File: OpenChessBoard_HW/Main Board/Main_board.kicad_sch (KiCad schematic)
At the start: 11 parts, among them U1 74HCT595, U2 74HCT595

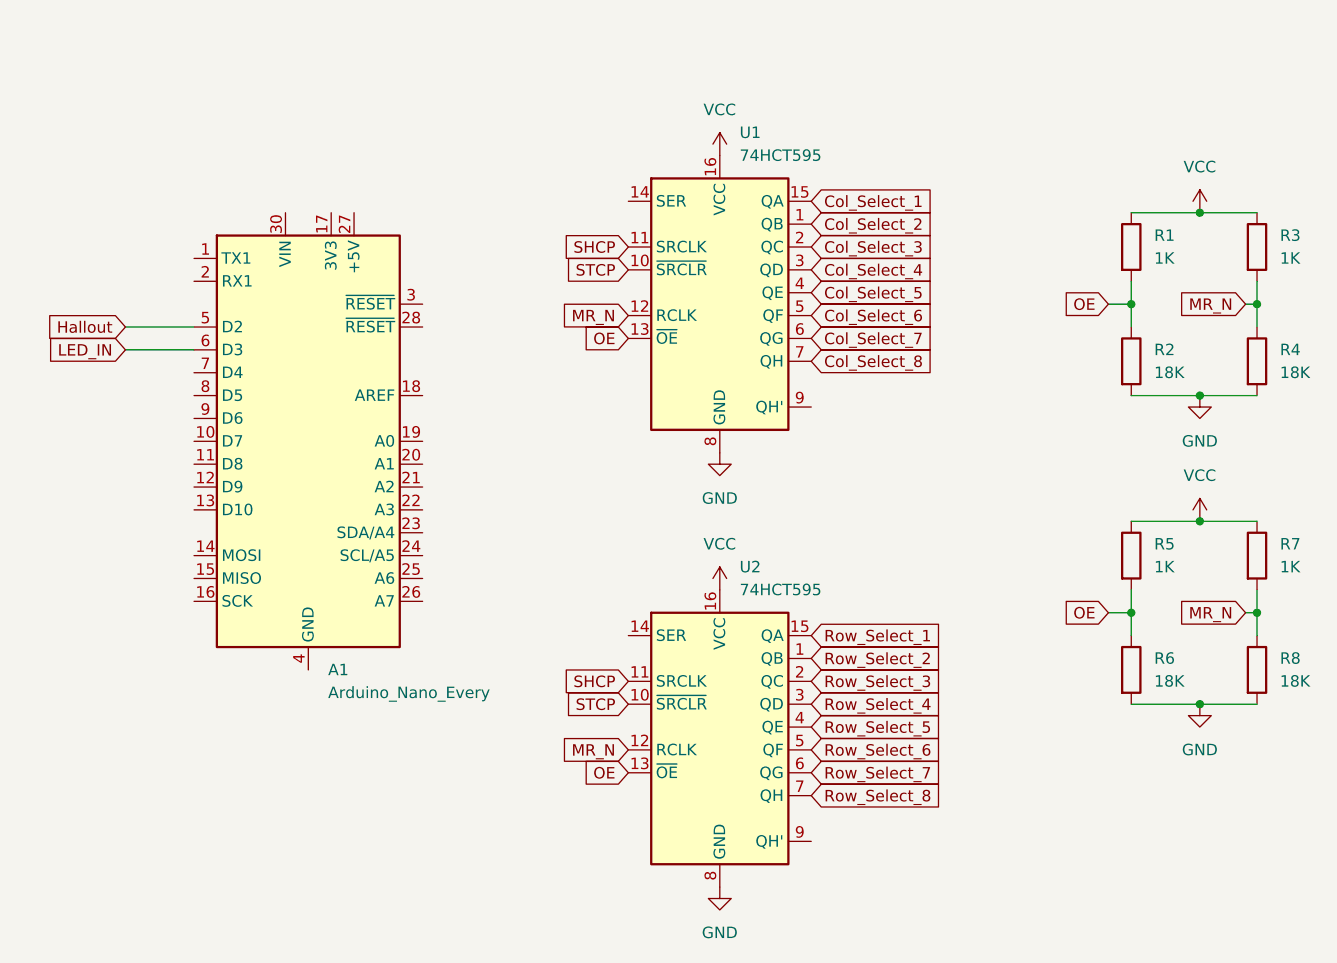
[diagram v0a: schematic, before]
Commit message: Populated Main board Schematic
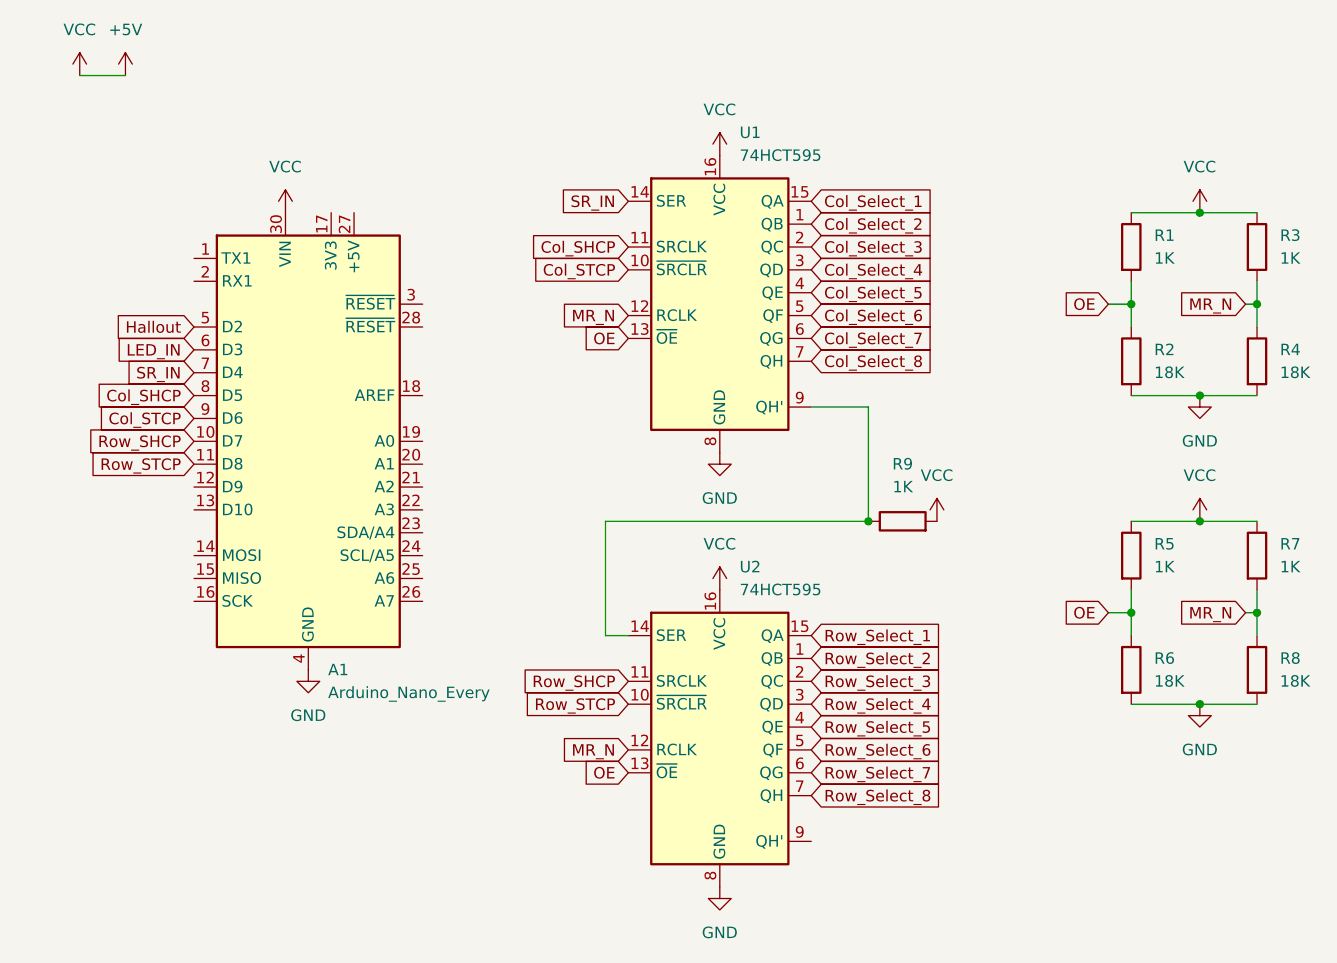
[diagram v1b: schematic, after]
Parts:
- added R9: 1K, Resistor_THT:R_Axial_DIN0204_L3.6mm_D1.6mm_P5.08mm_Horizontal, symbol Device:R
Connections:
- net VCC is gone; now on net +5V: R1.1, R3.1, R5.1, R7.1, U1.16 (VCC), U2.16 (VCC)
- net GND: now also A1.29 (GND), A1.4 (GND)
- net Row_SHCP: now reaches A1.10 (D7)
- net Row_SHCP: now also U2.11 (SRCLK)
- net Row_STCP: now reaches A1.11 (D8)
- net Row_STCP: now also U2.10 (~{SRCLR})
- net +5V: now reaches A1.30 (VIN)
- net +5V: now also R9.2
- net SR_IN: now reaches A1.7 (D4)
- net SR_IN: now also U1.14 (SER)
- net Col_SHCP: now reaches A1.8 (D5)
- net Col_SHCP: now also U1.11 (SRCLK)
- net Col_STCP: now reaches A1.9 (D6)
- net Col_STCP: now also U1.10 (~{SRCLR})
- net at U1.9 (QH'): now also U2.14 (SER), R9.1
- removed net SHCP: U1.11 (SRCLK), U2.11 (SRCLK)
- removed net STCP: U1.10 (~{SRCLR}), U2.10 (~{SRCLR})

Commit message: Update Main board to use 74HCT164 instead of 595
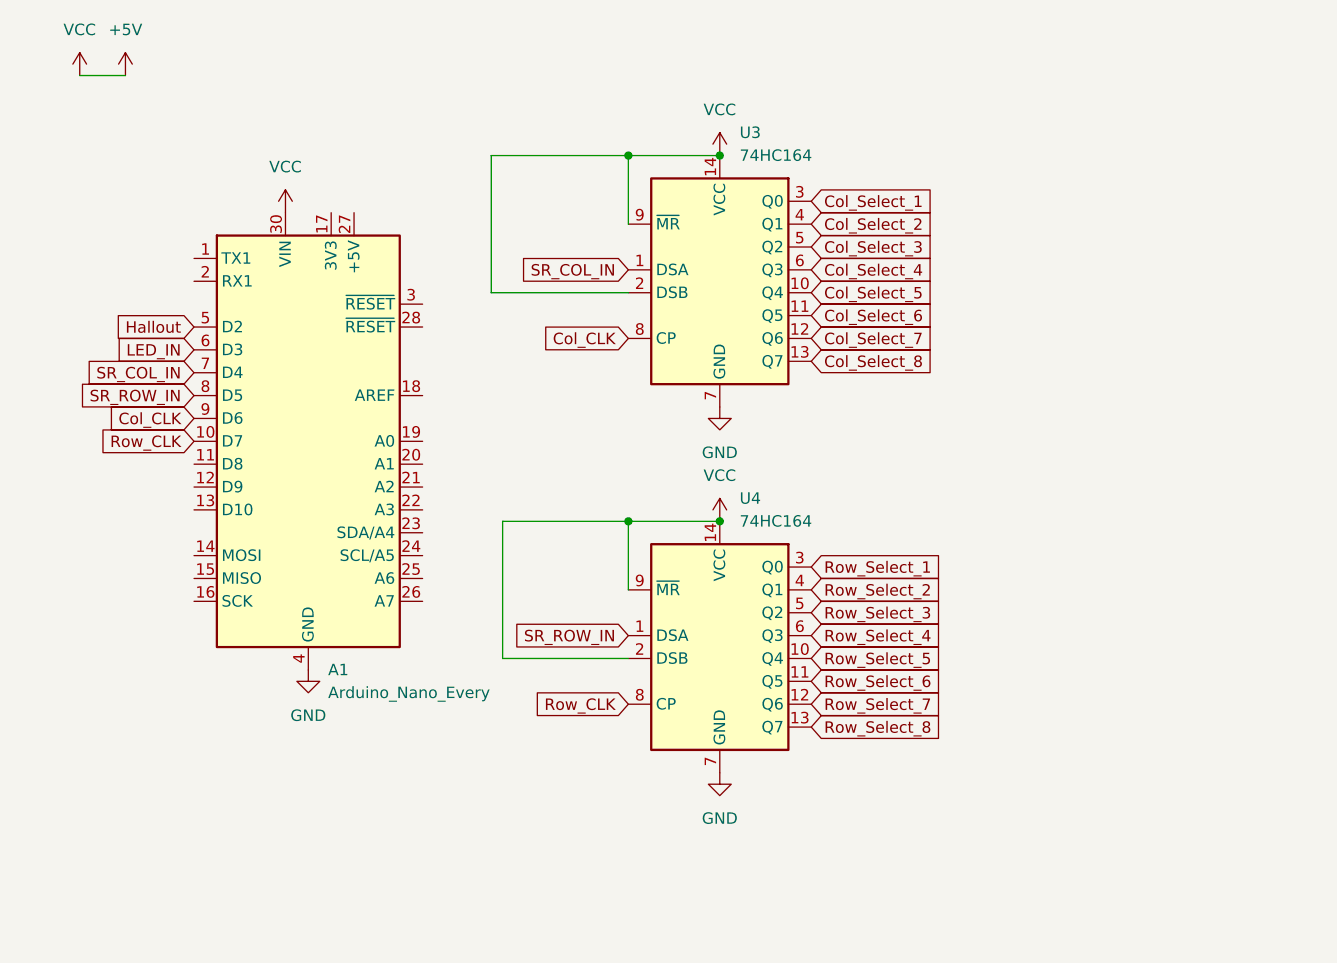
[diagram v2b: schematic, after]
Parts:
- removed R1, R3, R5, R7, R9: 1K, Resistor_THT:R_Axial_DIN0204_L3.6mm_D1.6mm_P5.08mm_Horizontal, symbol Device:R
- removed R2, R4, R6, R8: 18K, Resistor_THT:R_Axial_DIN0204_L3.6mm_D1.6mm_P5.08mm_Horizontal, symbol Device:R
- removed U1, U2: 74HCT595, Package_DIP:DIP-16_W7.62mm_Socket_LongPads, symbol 74xx:74HCT595
- added U3, U4: 74HC164, symbol 74xx:74HC164
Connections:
- net +5V: now also U3.14 (VCC), U3.2 (DSB), U3.9 (~{MR}), U4.14 (VCC), U4.2 (DSB), U4.9 (~{MR})
- net Col_Select_1: now also U3.3 (Q0)
- net Col_Select_2: now also U3.4 (Q1)
- net Col_Select_3: now also U3.5 (Q2)
- net Col_Select_4: now also U3.6 (Q3)
- net Col_Select_5: now also U3.10 (Q4)
- net Col_Select_6: now also U3.11 (Q5)
- net Col_Select_7: now also U3.12 (Q6)
- net Col_Select_8: now also U3.13 (Q7)
- net GND: now also U3.7 (GND), U4.7 (GND)
- net Row_Select_1: now also U4.3 (Q0)
- net Row_Select_2: now also U4.4 (Q1)
- net Row_Select_3: now also U4.5 (Q2)
- net Row_Select_4: now also U4.6 (Q3)
- net Row_Select_5: now also U4.10 (Q4)
- net Row_Select_6: now also U4.11 (Q5)
- net Row_Select_7: now also U4.12 (Q6)
- net Row_Select_8: now also U4.13 (Q7)
- net Col_SHCP renamed SR_ROW_IN
- net SR_ROW_IN: now also U4.1 (DSA)
- net Col_STCP renamed Col_CLK
- net Col_CLK: now also U3.8 (CP)
- net Row_SHCP renamed Row_CLK
- net Row_CLK: now also U4.8 (CP)
- net Row_STCP: no longer names the net of A1.11 (D8)
- net SR_IN renamed SR_COL_IN
- net SR_COL_IN: now also U3.1 (DSA)
